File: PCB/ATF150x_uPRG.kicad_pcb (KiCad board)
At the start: 2 copper layers, 38.1 x 22.9 mm, 29 parts, among them J1 Adafruit_2264, J2 Altera JTAG-A+VPP, SW1 SP3T, SW2 SPDT, U1 MAX662A

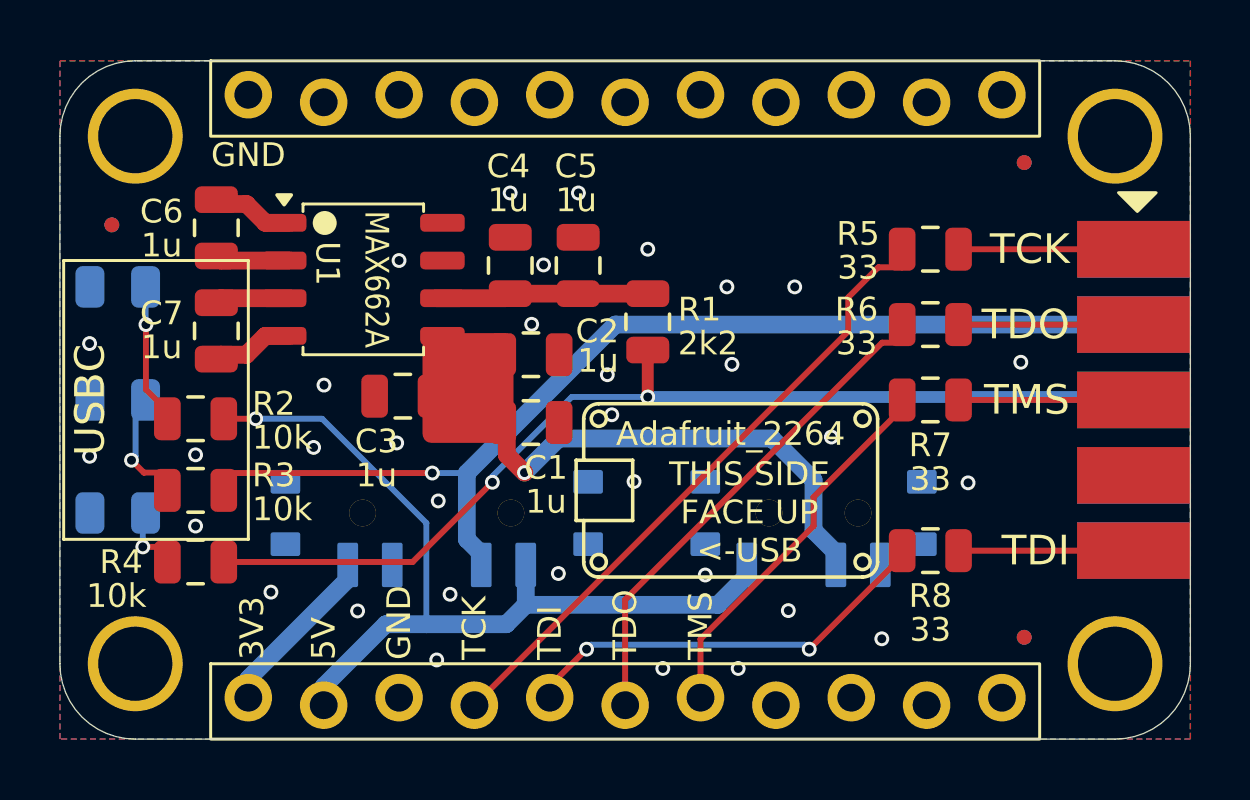
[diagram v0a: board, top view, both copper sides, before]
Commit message: make the jumper version the main version
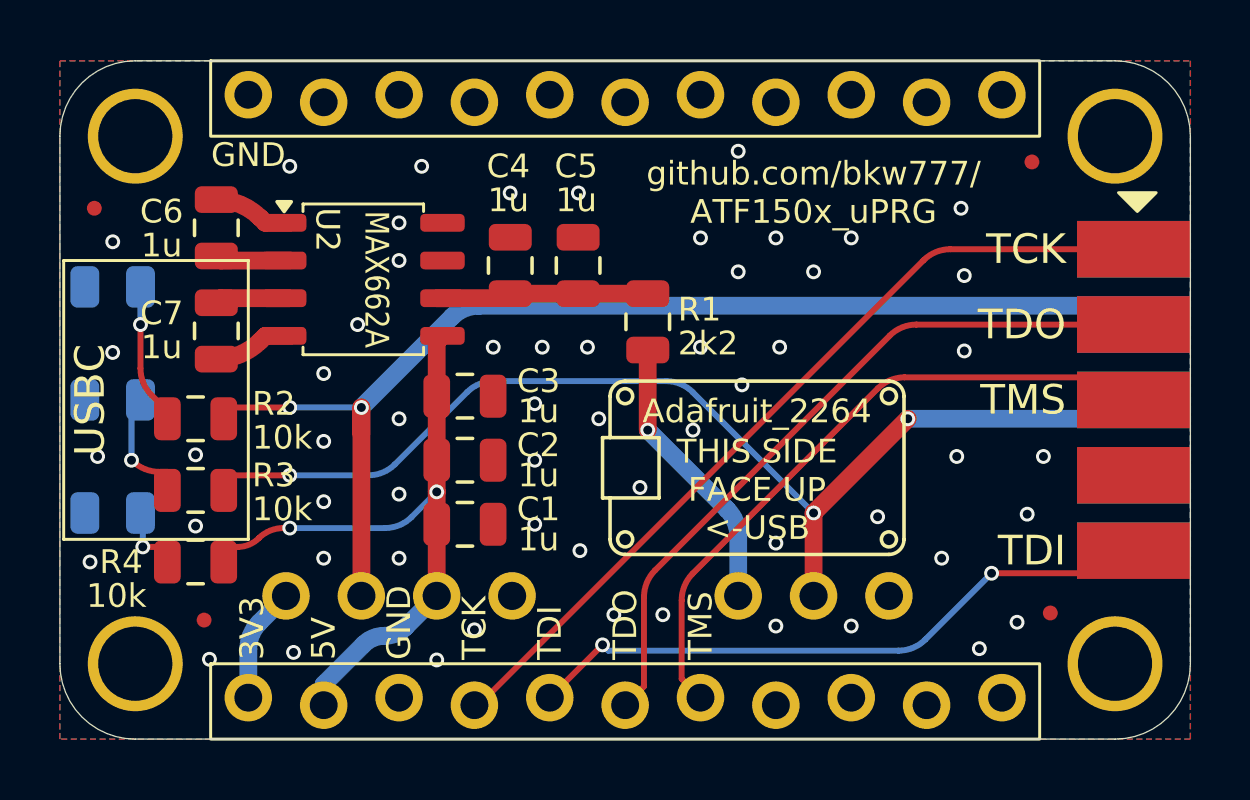
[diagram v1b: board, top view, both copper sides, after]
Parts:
- removed F0, F1, F2: Fiducial_0.5_1.0, 000_LOCAL:Fiducial_0.5_1.0
- removed R5, R6, R7, R8: 33, 000_LOCAL:R_0805
- removed SW1: SP3T, 000_LOCAL:CUS-13B pth
- removed SW2: SPDT, 000_LOCAL:CUS-12B pth
- added JP1: VCC, 000_LOCAL:PinHeader_1x04_P2.54mm_Horizontal, B.Cu at (142.2, 101.9)
- added JP2: VPP, 000_LOCAL:PinHeader_1x03_P2.54mm_Horizontal, B.Cu at (154.9, 101.9)
- added REF**: Fiducial_0.5_1.0, 000_LOCAL:Fiducial_0.5_1.0, F.Cu at (131.9, 102.7)
- LED1: value GREEN -> VCC
- LED2: value AMBER -> VPP
- LED3: value RED -> PWR
- moved C2 4.19 mm to (140.6, 97.3)
- moved C1 4.09 mm to (140.6, 99.4)
- moved C3 2.09 mm to (140.6, 95.1), turned to 0 degrees
- moved REF** 1.20 mm to (160.4, 102.4)
- moved REF** 0.81 mm to (128.2, 88.8)
- moved REF** 0.26 mm to (159.8, 87.2)
- moved LED1 0.17 mm to (128.8, 91.4)
- moved LED2 0.17 mm to (128.8, 95.2)
- moved LED3 0.17 mm to (128.8, 99.1)
- renumbered F3 to REF**, F5 to REF**, F4 to REF**, U1 to U2
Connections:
- C1 pad 1: Net-(SW2-B) -> +5V
- C2 pad 1: Net-(SW2-B) -> +5V
- C3 pad 1: Net-(SW2-B) -> +5V
- J1 pad 4: /TCK -> TCK
- J1 pad 5: /TDI -> TDI
- J1 pad 6: /TDO -> TDO
- J1 pad 7: /TMS -> TMS
- J2 pad 1: Net-(J2-TCK) -> TCK
- J2 pad 3: Net-(J2-TDO) -> TDO
- J2 pad 5: Net-(J2-TMS) -> TMS
- J2 pad 9: Net-(J2-TDI) -> TDI
- R1 pad 1: VPP -> Net-(JP2-Pad3)
- R2 pad 2: +5V -> VCC
- R3 pad 2: VCC -> VPP
- R4 pad 2: VPP -> +5V
- U2 pad 5: Net-(SW2-B) -> +5V
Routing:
- net TCK: track 0.00 -> 28.5 mm
- net TDO: track 0.00 -> 24.4 mm
- net TMS: track 0.00 -> 22.4 mm
- net TDI: track 0.00 -> 21.8 mm, vias 0 -> 2
- net /TCK: track 21.8 -> 0.00 mm
- net Net-(SW2-B): track 17.6 -> 0.00 mm, vias 1 -> 0
- net /TDO: track 17.1 -> 0.00 mm
- net /TDI: track 14.4 -> 0.00 mm, vias 2 -> 0
- net /TMS: track 12.8 -> 0.00 mm
- net Net-(JP2-Pad3): track 0.00 -> 9.49 mm, vias 0 -> 1
- net +5V: track 29.8 -> 22.8 mm, vias 1 -> 2
- net Net-(J2-TMS): track 5.90 -> 0.00 mm
- net Net-(J2-TDO): track 5.90 -> 0.00 mm
- net Net-(J2-TDI): track 5.90 -> 0.00 mm
- net Net-(J2-TCK): track 5.90 -> 0.00 mm
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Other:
- board text added: "12V"
- board text added: "ATF150x_uPRG"
- board text added: "N/C"
- board text added: "github.com/bkw777/ ATF150x_uPRG"
- board text added: "v${REVISION}"
- board text removed: "${COMMENT2}"
- board text removed: "${REVISION}"
- board text removed: "${TITLE}"
- board text removed: "5V TGT 3V3"
- board text removed: "OFF 12V"

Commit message: simplify, replace slide switches with jumpers, remove 33ohms
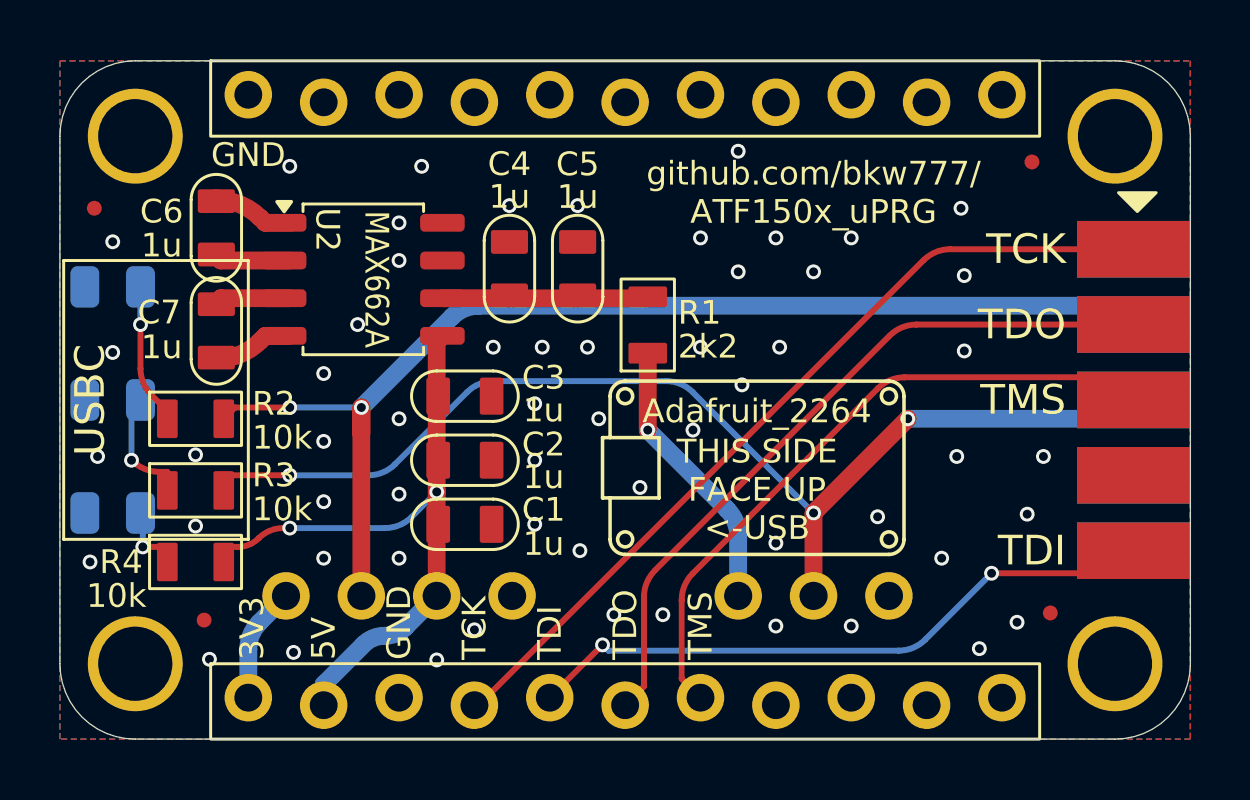
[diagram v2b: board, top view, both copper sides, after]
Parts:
- moved C4 0.11 mm to (142.2, 90.8)
- moved C5 0.11 mm to (144.4, 90.8)
- moved R1 0.11 mm to (146.8, 92.7)
